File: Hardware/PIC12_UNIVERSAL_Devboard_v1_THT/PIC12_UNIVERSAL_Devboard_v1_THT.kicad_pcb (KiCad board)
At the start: 2 copper layers, 0 parts

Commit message: PIC12 Universal Dev Board - Schematics - Changed Footprint of ICSP Header Layout - Defined Egde Cut, Imported Components from schematics
Signed-off-by: alexanderjg85 <alexanderjg85@gmail.com>
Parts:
- added C1: 1 uF, AJ_Passives:C6119929_C0805, F.Cu at (116.8, 129.1)
- added C2: 470nF, AJ_Passives:C13967_C0805, F.Cu at (116.8, 132.0)
- added C3: 1 uF, AJ_Passives:C6119929_C0805, F.Cu at (116.8, 135.0)
- added C4: 1 uF, AJ_Passives:C6119929_C0805, F.Cu at (116.8, 137.9)
- added C5: 100nF, AJ_Passives:C49678_C0805, F.Cu at (116.8, 140.9)
- added D1: SS14, Diode_SMD:D_SMA_Handsoldering, F.Cu at (124.4, 147.3)
- added D2: GREEN, LED_THT:LED_D3.0mm, F.Cu at (121.0, 130.3)
- added D3: YELLOW, LED_THT:LED_D3.0mm, F.Cu at (121.0, 135.8)
- added J2: Conn_PIC_ICSP_ICD, Connector_PinHeader_2.54mm:PinHeader_1x06_P2.54mm_Vertical, F.Cu at (98.6, 117.8)
- added J3: Screw_Terminal_01x02, TerminalBlock_Phoenix:TerminalBlock_Phoenix_MKDS-1,5-2-5.08_1x02_P5.08mm_Horizontal, F.Cu at (113.2, 121.7)
- added J4: Conn_01x07_Pin, Connector_PinHeader_2.54mm:PinHeader_1x07_P2.54mm_Vertical, F.Cu at (112.0, 129.9)
- added JP1: JP_PLED, TestPoint:TestPoint_2Pads_Pitch2.54mm_Drill0.8mm, F.Cu at (98.1, 148.6)
- added JP2: Jumper_3_Open, Connector_PinHeader_2.54mm:PinHeader_1x03_P2.54mm_Vertical, F.Cu at (116.5, 144.6)
- added JP3: JP_PLED, TestPoint:TestPoint_2Pads_Pitch2.54mm_Drill0.8mm, F.Cu at (98.1, 152.0)
- added R1: 680, Resistor_SMD:R_1206_3216Metric_Pad1.30x1.75mm_HandSolder, F.Cu at (128.2, 129.2)
- added R2: 10k, Resistor_SMD:R_1206_3216Metric_Pad1.30x1.75mm_HandSolder, F.Cu at (128.2, 132.6)
- added R3: 330, Resistor_SMD:R_1206_3216Metric_Pad1.30x1.75mm_HandSolder, F.Cu at (128.2, 135.9)
- added SW1: SW_RESET, Button_Switch_SMD:SW_SPST_PTS647_Sx38, F.Cu at (123.5, 141.8)
- added TP1: VDD, TestPoint:TestPoint_Pad_D1.5mm, F.Cu at (98.1, 134.5)
- added TP10: GP4, TestPoint:TestPoint_Pad_D1.5mm, F.Cu at (105.2, 138.1)
- added TP11: GP5, TestPoint:TestPoint_Pad_D1.5mm, F.Cu at (105.2, 141.6)
- added TP2: PLED, TestPoint:TestPoint_Pad_D1.5mm, F.Cu at (98.1, 138.1)
- added TP3: VCC, TestPoint:TestPoint_Pad_D1.5mm, F.Cu at (98.1, 141.6)
- added TP4: VCC3_3, TestPoint:TestPoint_Pad_D1.5mm, F.Cu at (98.1, 145.2)
- added TP5: VCC5, TestPoint:TestPoint_Pad_D1.5mm, F.Cu at (101.6, 134.5)
- added TP6: GND, TestPoint:TestPoint_Pad_D1.5mm, F.Cu at (101.6, 138.1)
- added TP7: DAT, TestPoint:TestPoint_Pad_D1.5mm, F.Cu at (101.6, 141.6)
- added TP8: CLK, TestPoint:TestPoint_Pad_D1.5mm, F.Cu at (101.6, 145.2)
- added TP9: LED, TestPoint:TestPoint_Pad_D1.5mm, F.Cu at (105.2, 134.5)
- added U1: PIC12F617-xP, Package_DIP:DIP-8_W7.62mm, F.Cu at (123.5, 117.5)
- added U2: 78L05G-AB3-R, AJ_Power:C71136_SOT-89-3_L4_5-W2_5-P1_50-LS4_2-BR, F.Cu at (106.2, 149.9)
- added U3: XC6206-3.3V_C3015484, AJ_Power:C3015484_SOT-23-3_L2_9-W1_3-P0_95-LS2_4-BR, F.Cu at (129.8, 140.6)
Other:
- board outline added: 70 x 40 mm

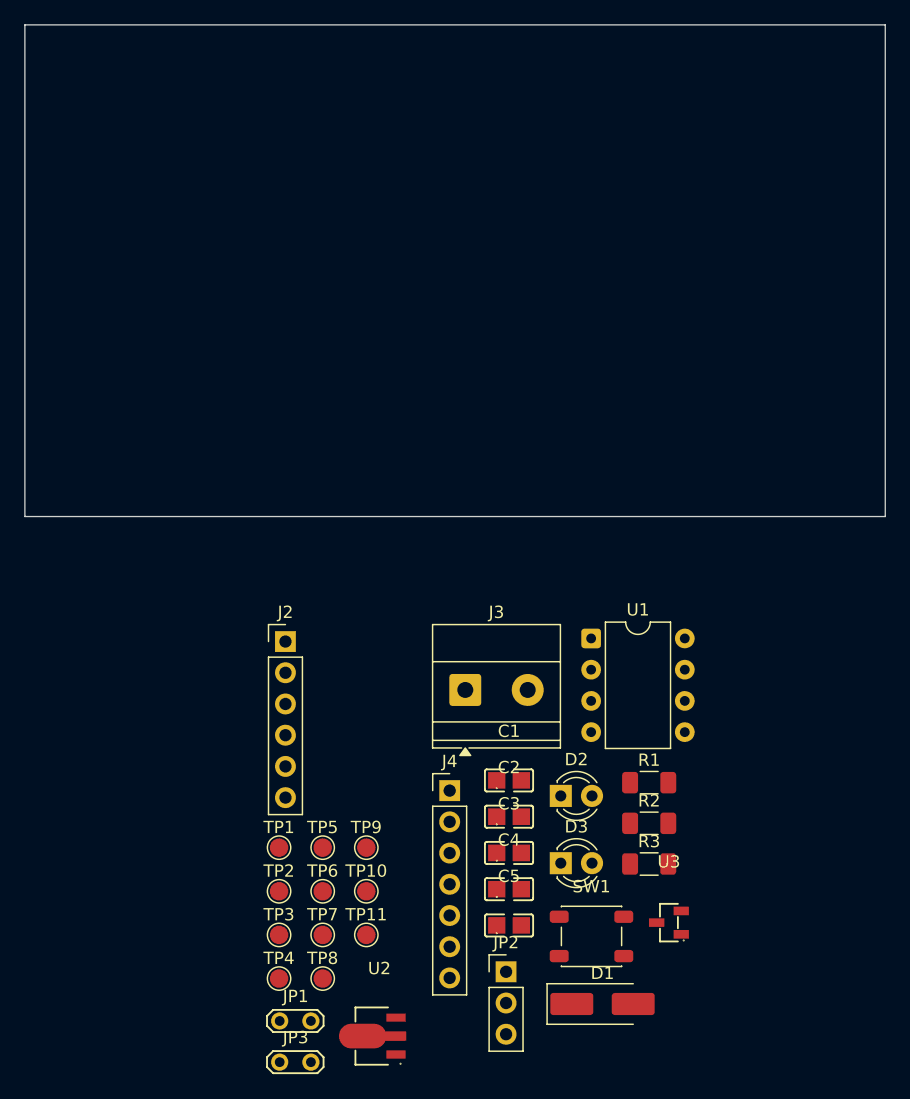
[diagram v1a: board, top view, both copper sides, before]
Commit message: IC12 Universal Dev Board - Layout - Finished Initial Component Placement
Signed-off-by: alexanderjg85 <alexanderjg85@gmail.com>
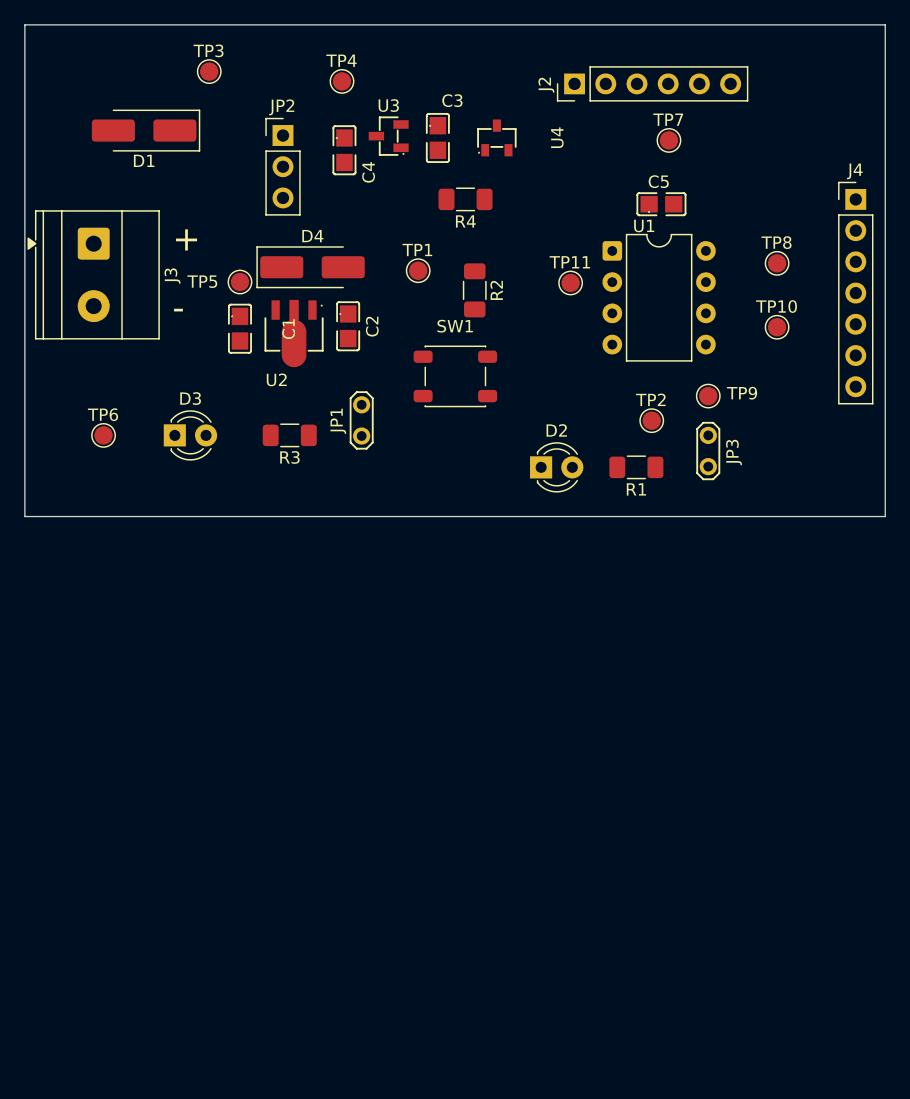
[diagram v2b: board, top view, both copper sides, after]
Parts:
- added D4: SS14, Diode_SMD:D_SMA_Handsoldering, F.Cu at (100.8, 87.3)
- added R4: 10k, Resistor_SMD:R_1206_3216Metric_Pad1.30x1.75mm_HandSolder, F.Cu at (113.2, 81.8)
- added U4: SI2301-A1SHB, AJ_Transistors:C28642376_SOT-23-3_L2_9-W1_3-P1_90-LS2_4-BR, F.Cu at (115.8, 76.8)
- JP3: value JP_PLED -> JP_SLED
- TP2: value PLED -> SLED
- moved D1 80.3 mm to (87.1, 76.2), turned to 180 degrees
- moved TP4 73.2 mm to (103.2, 72.2)
- moved TP7 70.5 mm to (129.8, 77.0)
- moved TP3 70.5 mm to (92.4, 71.4)
- moved JP2 70.4 mm to (98.4, 76.6)
- moved TP8 68.9 mm to (138.6, 87.0)
- moved U3 67.9 mm to (107.0, 76.7)
- moved JP3 61.8 mm to (133.0, 101.0), turned to -90 degrees
- moved C4 61.6 mm to (103.4, 77.8), turned to -90 degrees
- moved C5 60.0 mm to (129.2, 82.2)
- moved C3 58.5 mm to (111.0, 76.8), turned to -90 degrees
- moved J4 58.4 mm to (145.0, 81.8)
- moved U2 58.1 mm to (99.3, 92.2), turned to 90 degrees
- moved TP10 56.8 mm to (138.6, 92.2)
- moved TP11 55.6 mm to (121.8, 88.6)
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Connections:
- C3 pad 1: VDD -> Net-(U3-VOUT)
- U3 pad 2: VDD -> Net-(U3-VOUT)
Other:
- board text added: "+"
- board text added: "-"
- board text added: "Alexander Jaeger 2026"
- board text added: "Pic12 Universal Devboard V1 THT"

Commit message: PIC12 Universal Dev Board - Layout - Finished Routing
Signed-off-by: alexanderjg85 <alexanderjg85@gmail.com>
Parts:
- added REF**: MountingHole_2.7mm_M2.5, MountingHole:MountingHole_2.7mm_M2.5, F.Cu at (81.0, 71.2)
- added REF**: MountingHole_2.7mm_M2.5, MountingHole:MountingHole_2.7mm_M2.5, F.Cu at (143.8, 104.0)
- added REF**: MountingHole_2.7mm_M2.5, MountingHole:MountingHole_2.7mm_M2.5, F.Cu at (81.0, 104.0)
- added REF**: MountingHole_2.7mm_M2.5, MountingHole:MountingHole_2.7mm_M2.5, F.Cu at (143.8, 71.2)
- moved TP6 3.11 mm to (86.0, 98.8)
- moved TP10 1.71 mm to (140.3, 92.0)
- moved TP4 0.28 mm to (103.4, 72.0)
- moved U3 0.15 mm to (107.0, 76.8)
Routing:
- net VDD: track 0.00 -> 94.5 mm
- net GND: track 0.00 -> 61.5 mm, vias 0 -> 27
- net PIC_RST: track 0.00 -> 45.6 mm, vias 0 -> 2
- net VCC_5: track 0.00 -> 38.8 mm
- net PIC_ICSPCLK: track 0.00 -> 32.5 mm, vias 0 -> 2
- net PIC_ICSPDAT: track 0.00 -> 31.7 mm, vias 0 -> 2
- net PIC_GP5: track 0.00 -> 28.3 mm, vias 0 -> 2
- net PIC_LED: track 0.00 -> 21.4 mm
- net PIC_GP4: track 0.00 -> 20.5 mm, vias 0 -> 1
- net VCC: track 0.00 -> 18.2 mm
- net VCC_3_3: track 0.00 -> 12.5 mm
- net Net-(D1-A): track 0.00 -> 9.86 mm
- net Net-(JP3-B): track 0.00 -> 8.16 mm
- net Net-(U3-VOUT): track 0.00 -> 7.75 mm
- net Net-(D3-A): track 0.00 -> 5.26 mm
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- added copper zone on B.Cu, net GND

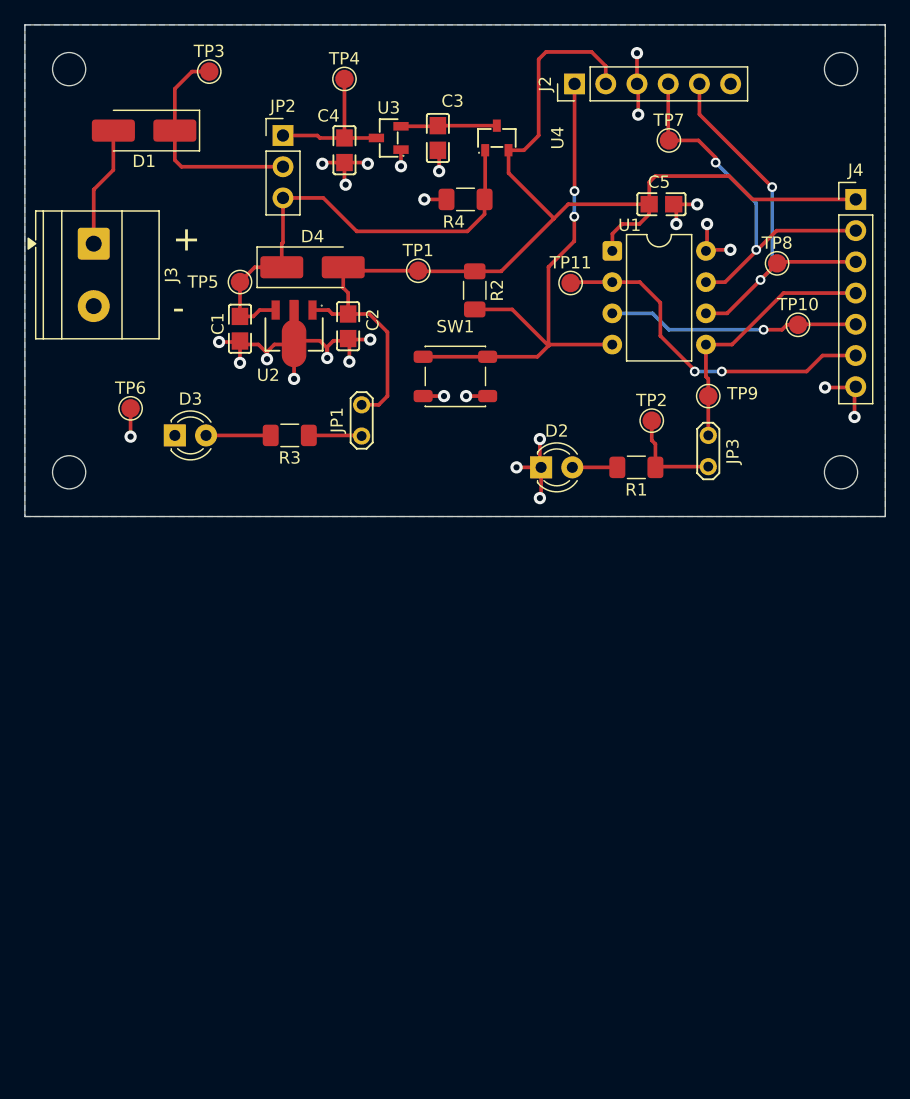
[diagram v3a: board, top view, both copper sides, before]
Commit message: PIC12 Universal Dev Board - Layout - Finished Silk Screen
Signed-off-by: alexanderjg85 <alexanderjg85@gmail.com>
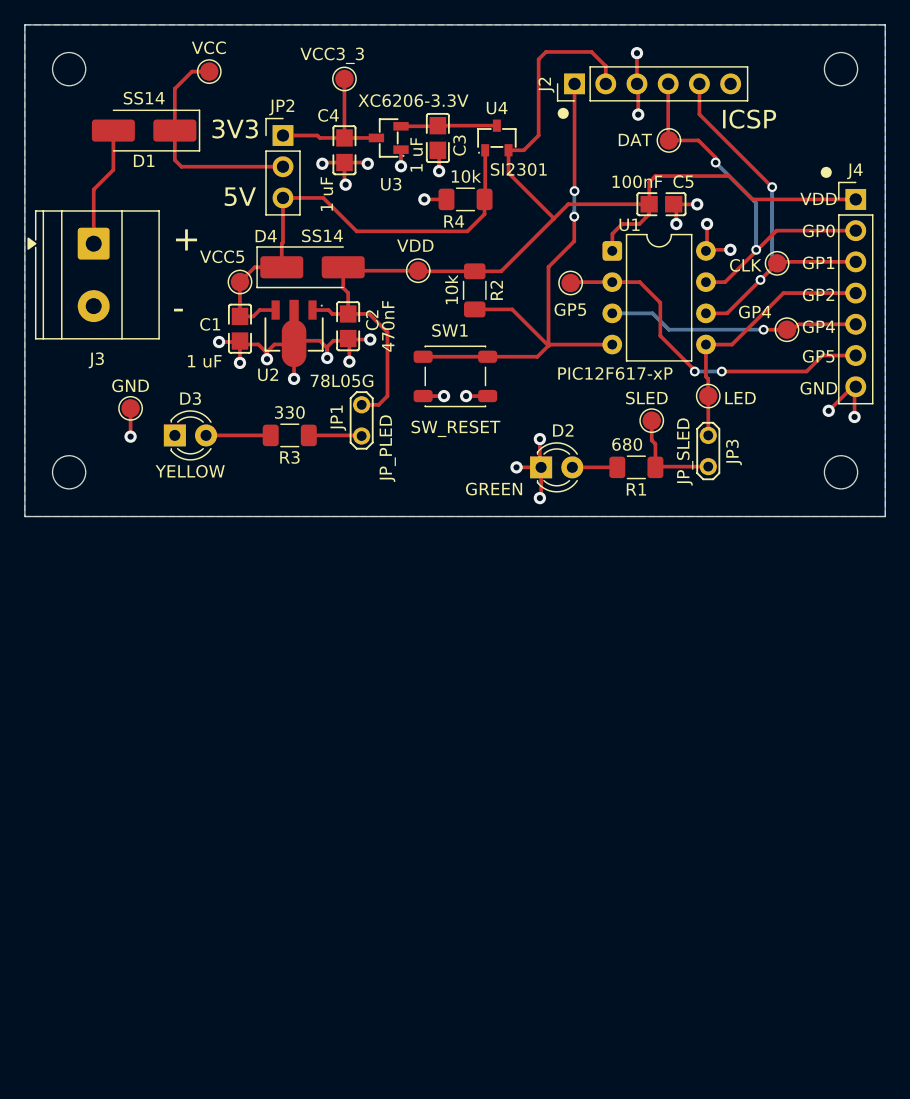
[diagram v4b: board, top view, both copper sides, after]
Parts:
- U2: value 78L05G-AB3-R -> 78L05G
- U3: value XC6206-3.3V_C3015484 -> XC6206-3.3V
- U4: value SI2301-A1SHB -> SI2301
- moved TP10 0.98 mm to (139.4, 92.4)
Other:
- board text added: "3V3"
- board text added: "5V"
- board text added: "GND"
- board text added: "GP0"
- board text added: "GP1"
- board text added: "GP2"
- board text added: "GP4"
- board text added: "GP5"
- board text added: "ICSP"
- board text added: "VDD"
